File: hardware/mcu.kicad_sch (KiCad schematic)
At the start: 44 parts, among them J13 USB_C_Receptacle_USB2.0_14P, J14 SM03B-SRSS-TB, SW4 SW_BOOT, SW5 SW_RESET, U3 W25Q128JVS, U4 W25Q128JVS, U5 AP2112K-3.3, U6 RP2350A-QFN60, Y1 ABM8-272-T3

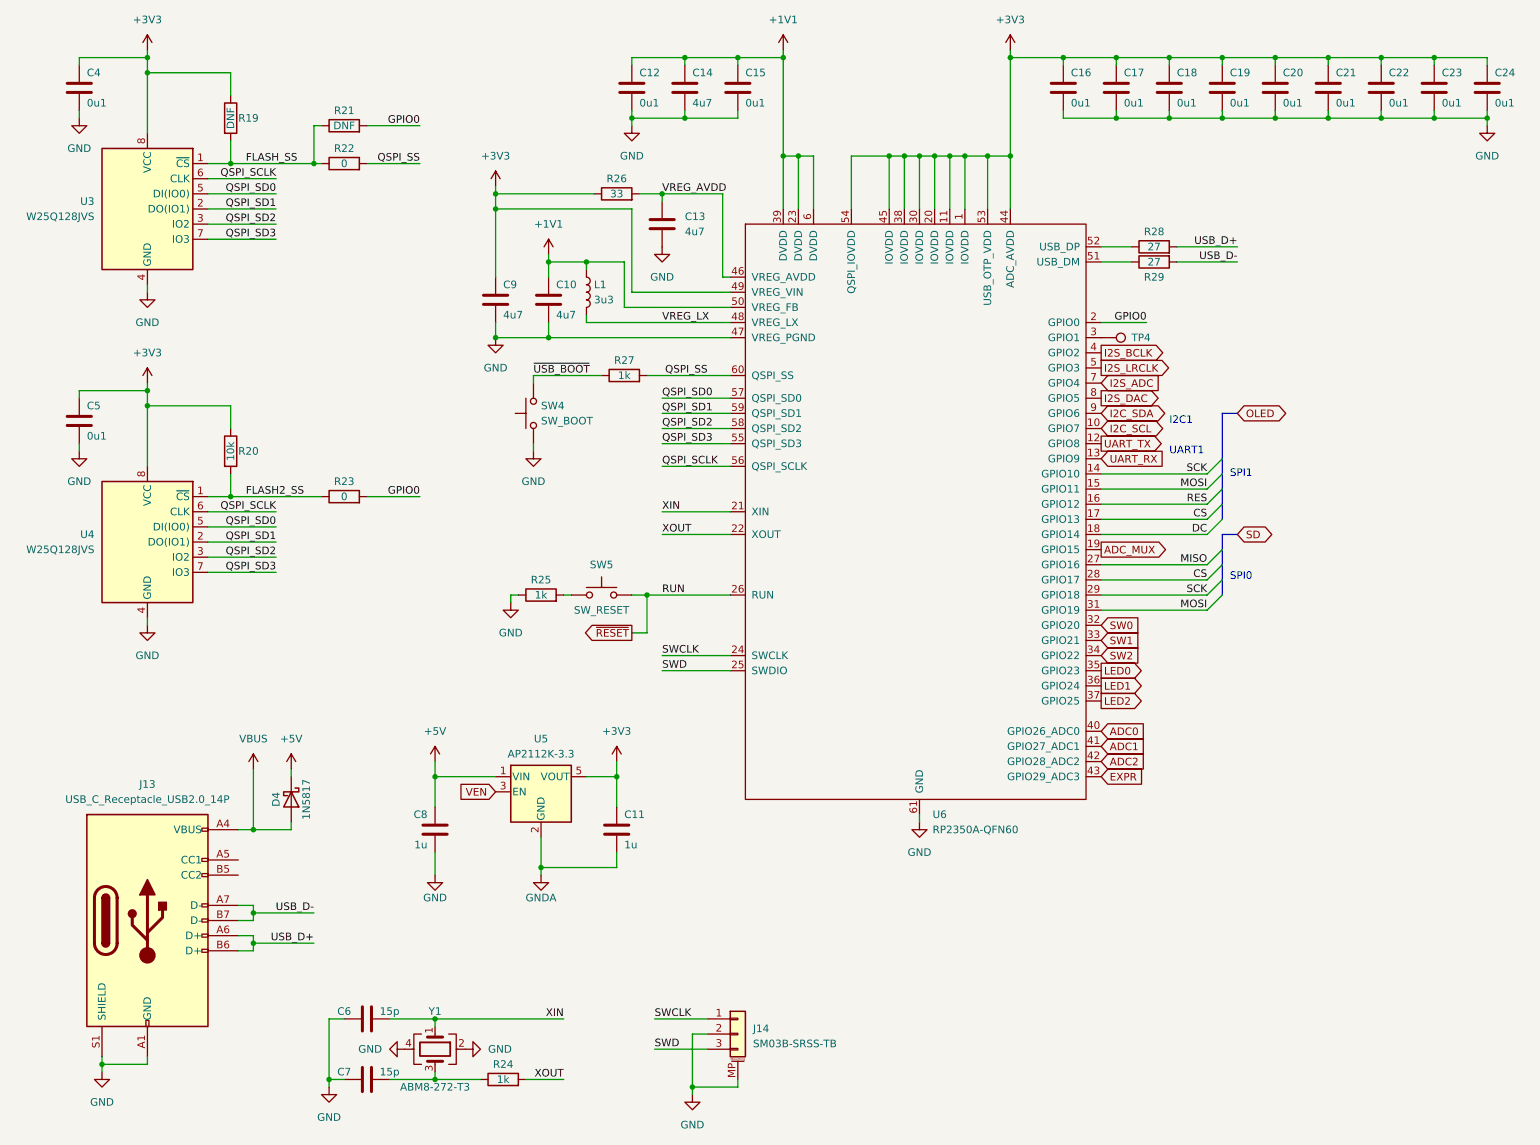
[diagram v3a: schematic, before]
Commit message: Footprint assignments
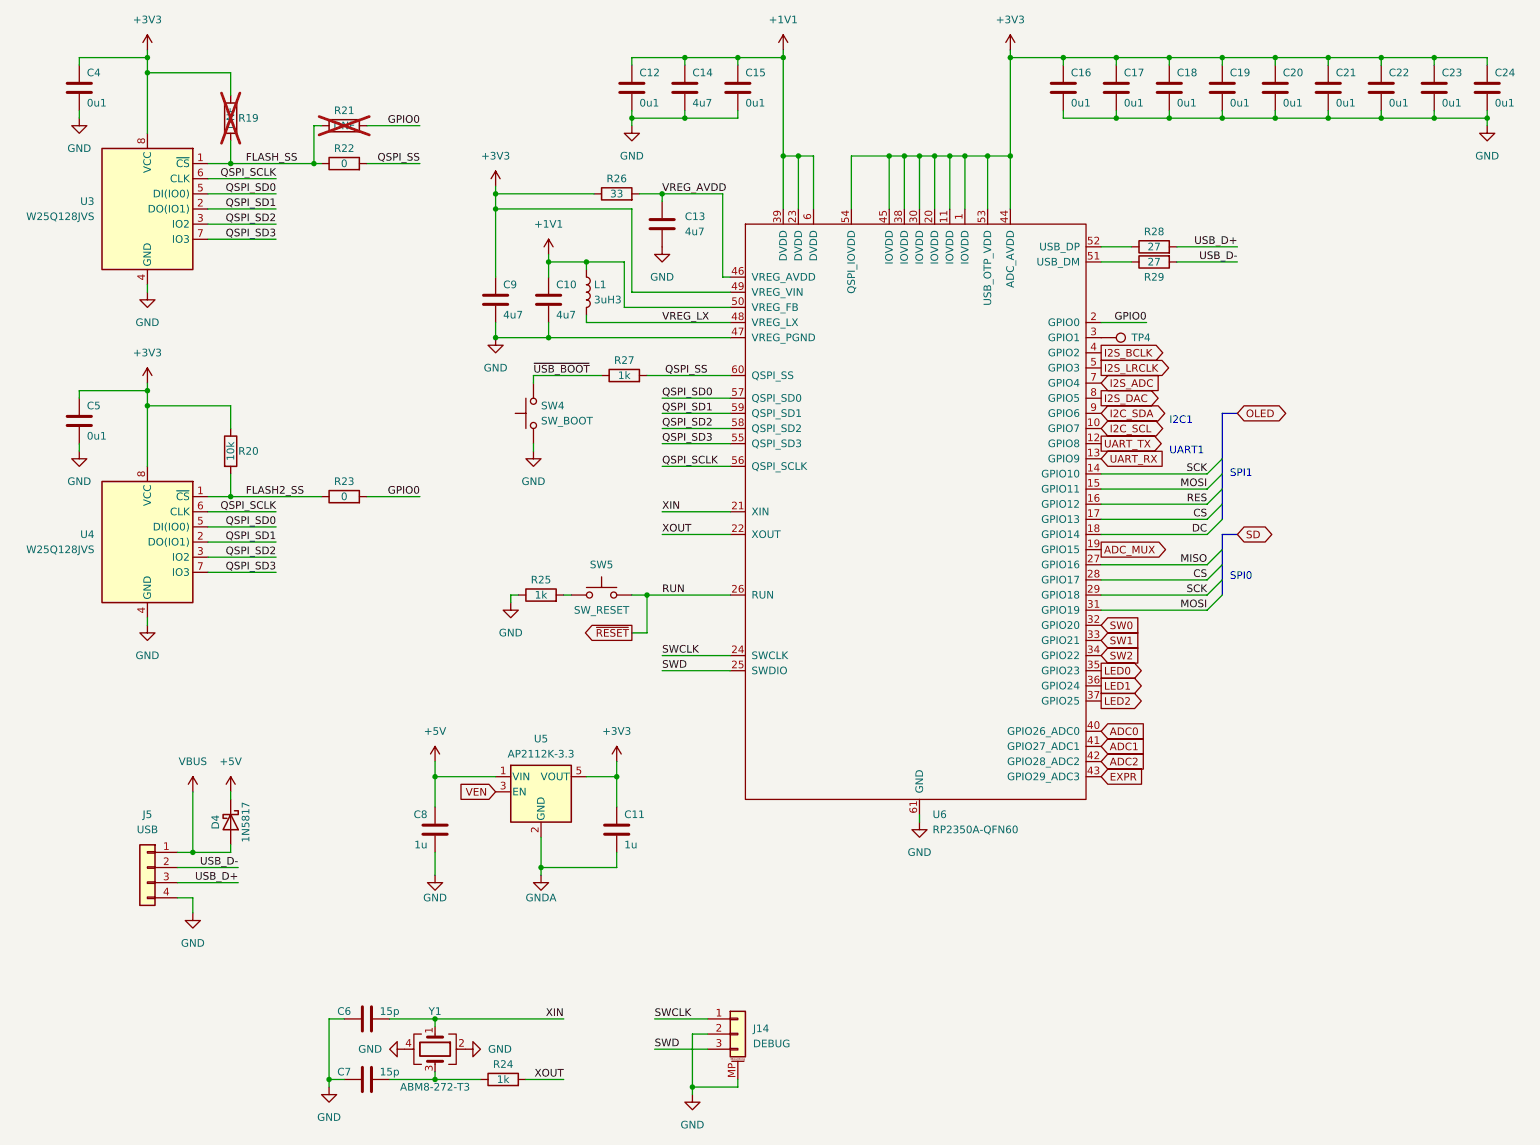
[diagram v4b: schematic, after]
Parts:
- removed J13: USB_C_Receptacle_USB2.0_14P, symbol Connector:USB_C_Receptacle_USB2.0_14P
- added J5: USB, Connector_JST:JST_PH_B4B-PH-K_1x04_P2.00mm_Vertical, symbol Connector_Generic:Conn_01x04
- C10, C11, C13, C14, C8, C9: footprint (none) -> Capacitor_SMD:C_0603_1608Metric
- C12, C15, C16, C17, C18, C19, C20, C21, C22, C23, C24, C4, C5, C6, C7: footprint (none) -> Capacitor_SMD:C_0402_1005Metric
- D4: footprint (none) -> Diode_SMD:D_SOD-123
- J14: value SM03B-SRSS-TB -> DEBUG; footprint (none) -> Connector_JST:JST_SH_SM03B-SRSS-TB_1x03-1MP_P1.00mm_Horizontal
- L1: value 3u3 -> 3uH3; footprint (none) -> Inductor_SMD:L_0603_1608Metric
- R19, R21: footprint (none) -> Resistor_SMD:R_0402_1005Metric; now not fitted
- R20, R22, R23, R24, R26, R27: footprint (none) -> Resistor_SMD:R_0402_1005Metric
- R25, R28, R29: footprint (none) -> Resistor_SMD:R_0603_1608Metric
- SW4, SW5: footprint (none) -> Button_Switch_SMD:SW_Push_1P1T_XKB_TS-1187A
- TP4: footprint (none) -> TestPoint:TestPoint_Pad_D1.5mm
- Y1: footprint (none) -> Crystal:Crystal_SMD_3225-4Pin_3.2x2.5mm
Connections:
- net GND: now also J5.4 (Pin_4)
- net USB_D+: now also J5.3 (Pin_3)
- net USB_D-: now also J5.2 (Pin_2)
- net VBUS: now also J5.1 (Pin_1)
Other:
- moved on the sheet: D4

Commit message: Change connectors to JST SH
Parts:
- J5: footprint Connector_JST:JST_PH_B4B-PH-K_1x04_P2.00mm_Vertical -> Connector_JST:JST_SH_SM04B-SRSS-TB_1x04-1MP_P1.00mm_Horizontal
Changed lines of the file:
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@@
 			)
 		)
-		(property "Footprint" "Connector_JST:JST_PH_B4B-PH-K_1x04_P2.00mm_Vertical"
+		(property "Footprint" "Connector_JST:JST_SH_SM04B-SRSS-TB_1x04-1MP_P1.00mm_Horizontal"
 			(at 34.29 157.48 0)
 			(effects

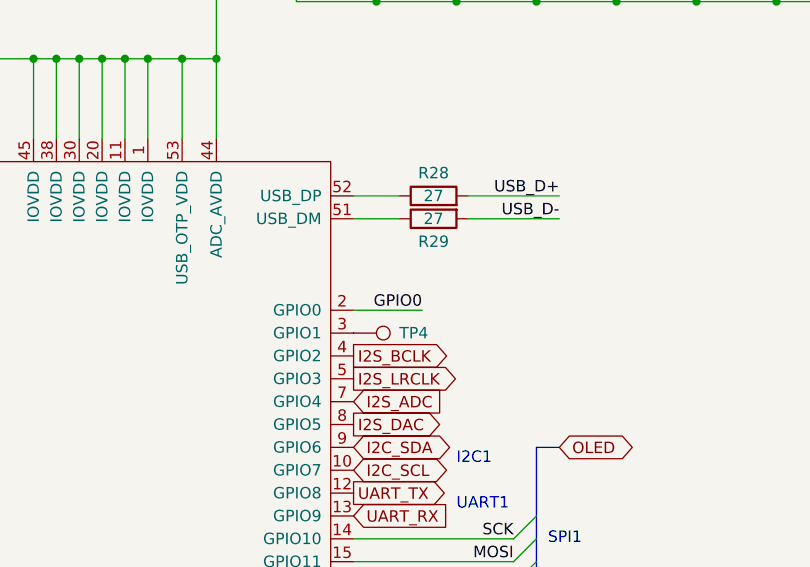
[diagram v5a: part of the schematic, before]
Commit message: Add test point to GPIO0
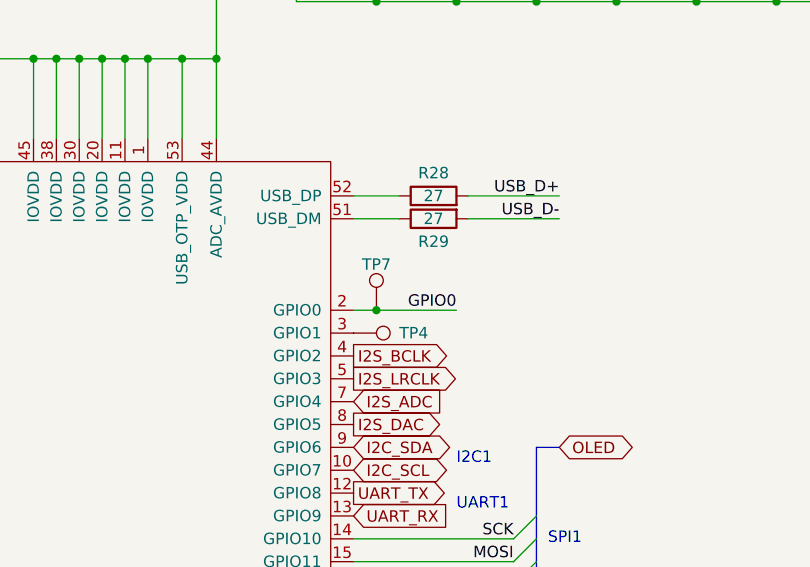
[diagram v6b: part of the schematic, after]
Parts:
- added TP7: TestPoint, TestPoint:TestPoint_Pad_D1.5mm, symbol Connector:TestPoint
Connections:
- net GPIO0: now also TP7.1
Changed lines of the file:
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@@
 	)
 	(junction
+		(at 196.85 66.04)
+		(diameter 0)
+		(color 0 0 0 0)
+	)
+	(junction
 		(at 232.41 21.59)
 		(diameter 0)
@@
 	(wire
 		(pts
-			(xy 194.31 66.04) (xy 201.93 66.04)
+			(xy 194.31 66.04) (xy 196.85 66.04)
 		)
 		(stroke
@@
 	(wire
 		(pts
+			(xy 196.85 66.04) (xy 205.74 66.04)
+		)
+		(stroke
+			(width 0)
+			(type default)
+		)
+	)
+	(wire
+		(pts
 			(xy 120.65 121.92) (xy 132.08 121.92)
 		)
@@
 	)
 	(label "GPIO0"
-		(at 201.93 66.04 180)
+		(at 205.74 66.04 180)
 		(effects
 			(font
@@
 					(unit 1)
 				)
+			)
+		)
+	)
+	(symbol
+		(lib_id "Connector:TestPoint")
+		(at 196.85 66.04 0)
+		(unit 1)
+		(exclude_from_sim no)
+		(in_bom yes)
+		(on_board yes)
+		(dnp no)
+		(property "Reference" "TP7"
+			(at 196.85 60.96 0)
+			(effects
+				(font
+					(size 1.27 1.27)
+				)
+			)
+		)
+		(property "Value" "TestPoint"
+			(at 199.39 64.0079 0)
+			(effects
+				(font
+					(size 1.27 1.27)
+				)
+				(justify left)
+				(hide yes)
+			)
+		)
+		(property "Footprint" "TestPoint:TestPoint_Pad_D1.5mm"
+			(at 201.93 66.04 0)
+			(effects
+				(font
+					(size 1.27 1.27)
+				)
+				(hide yes)
+			)
+		)
+		(property "Datasheet" "~"
+			(at 201.93 66.04 0)
+			(effects
+				(font
+					(size 1.27 1.27)
+				)
+				(hide yes)
+			)
+		)
+		(property "Description" "test point"
+			(at 196.85 66.04 0)
+			(effects
+				(font
+					(size 1.27 1.27)
+				)
+				(hide yes)
+			)
+		)
+		(pin "1"
+		)
+		(instances
+			(project "Zero-Stomp"
+				(path "/8c8d5801-9c58-4283-98ac-c6a8e7250e15/18032a8d-c86f-4e94-b2bf-e3bf4b84450f"
+					(reference "TP7")
+					(unit 1)
+				)
